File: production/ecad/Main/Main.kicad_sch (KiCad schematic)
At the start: 2 parts, among them J8 61301611821, J9 61301611821

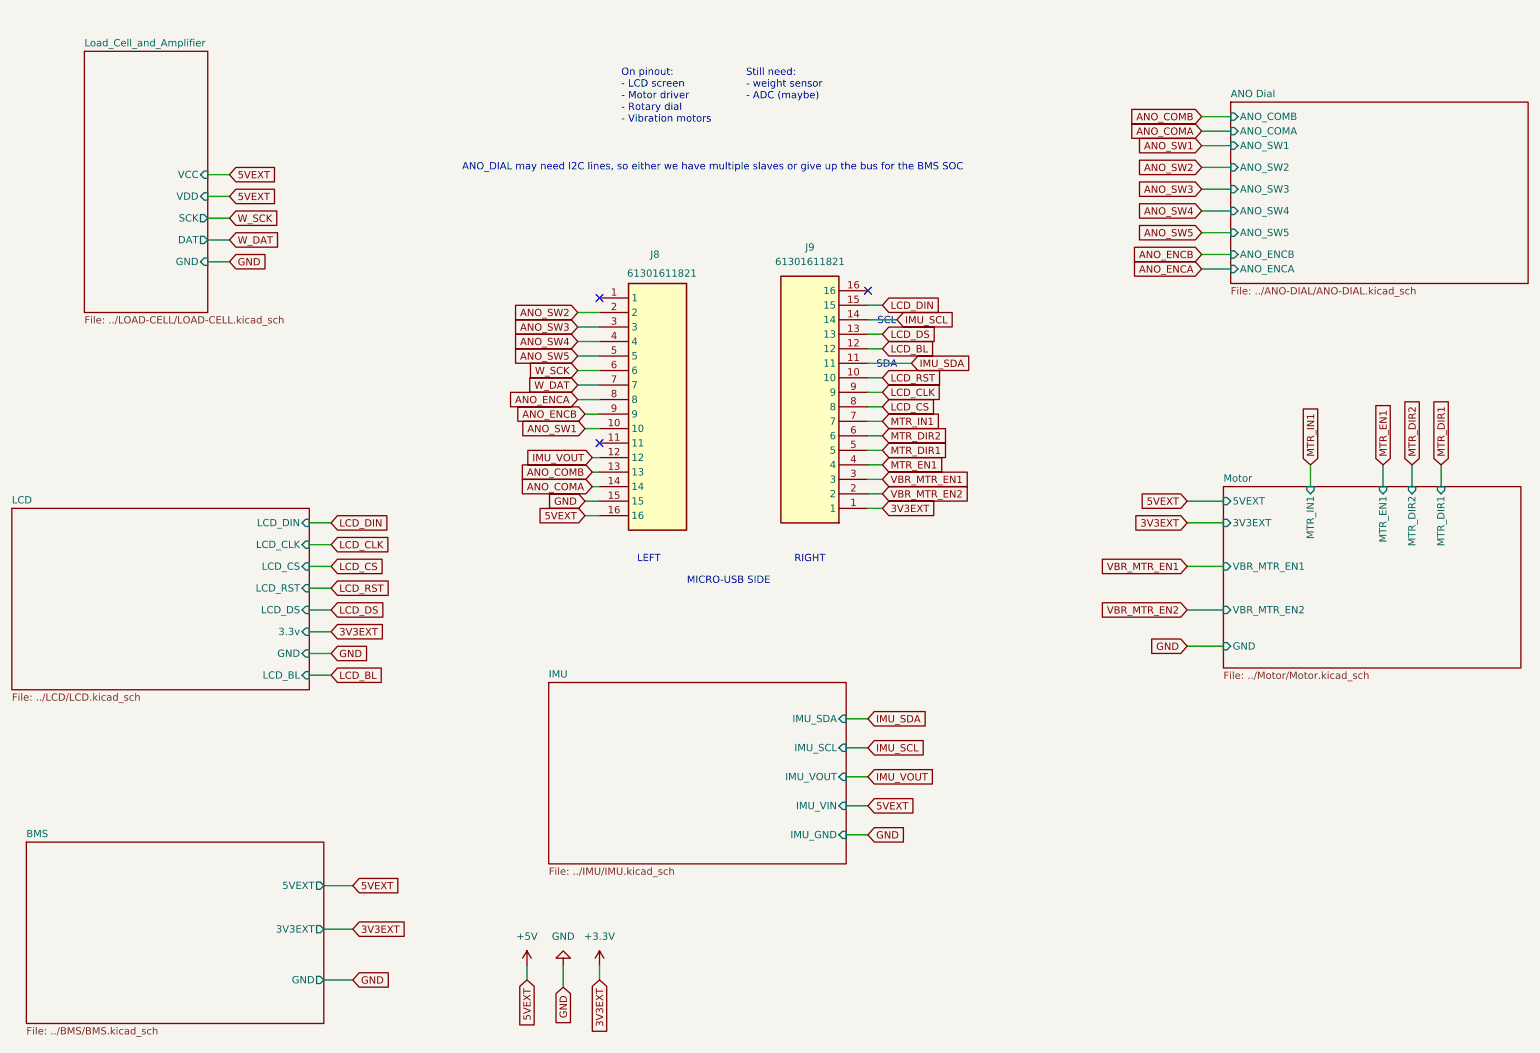
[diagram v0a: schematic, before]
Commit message: added connector for pisugar
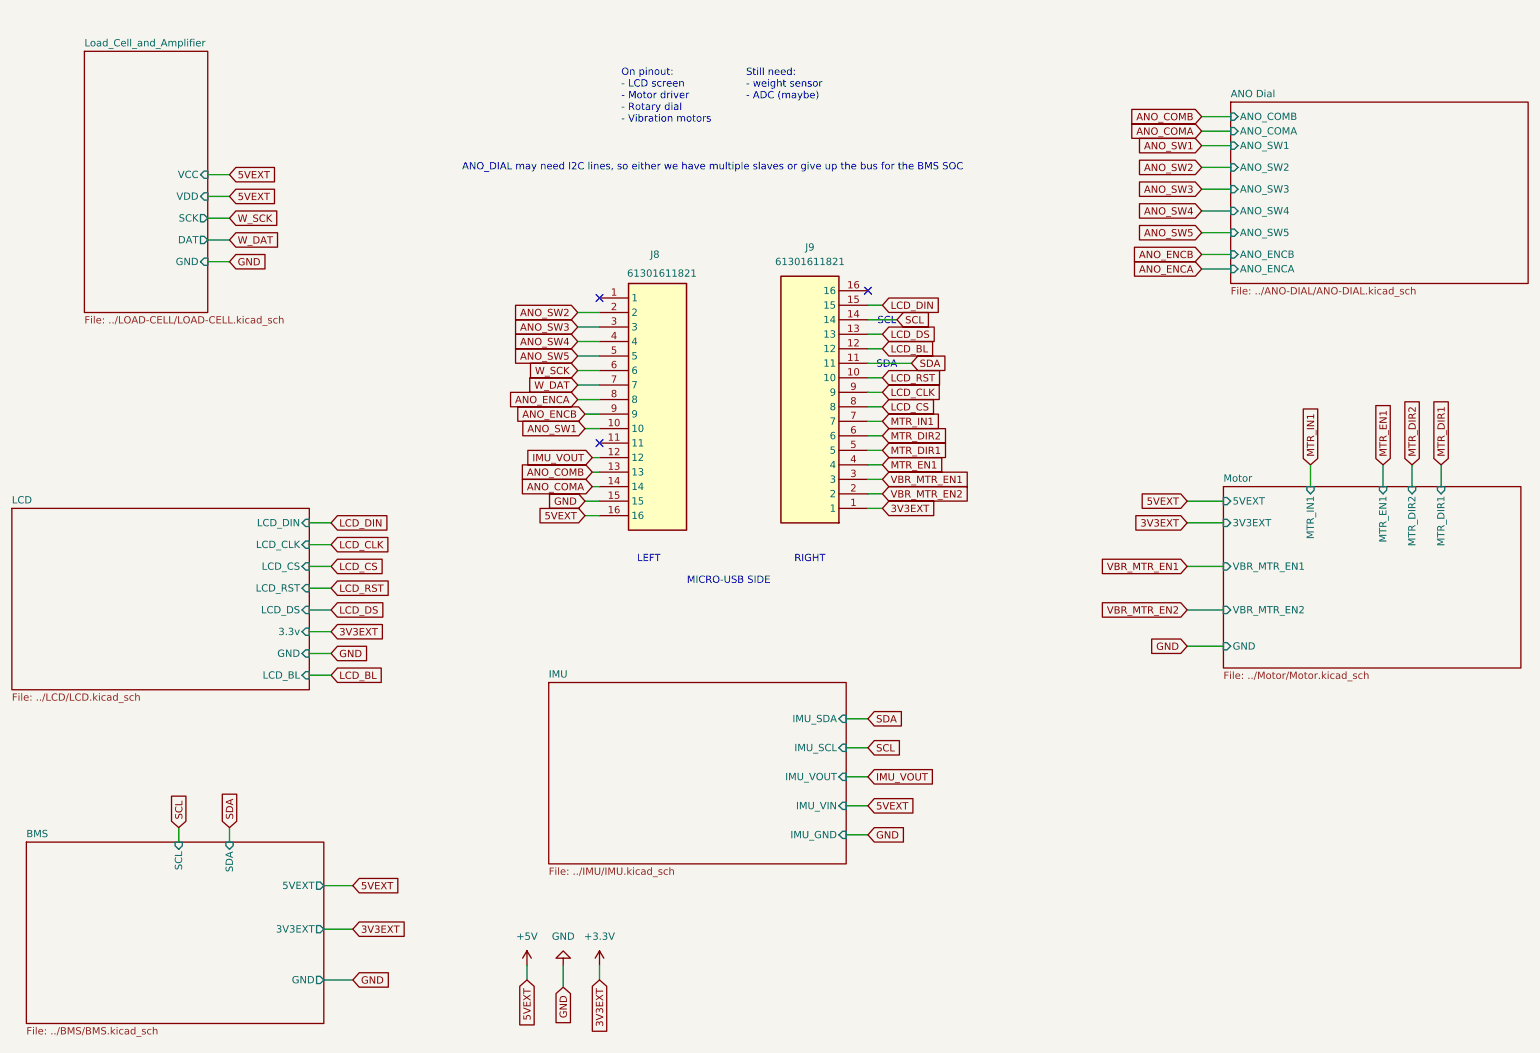
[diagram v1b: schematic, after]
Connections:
- net IMU_SCL renamed SCL
- net IMU_SDA renamed SDA
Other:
- sheet BMS ports: added SCL, SDA; removed none
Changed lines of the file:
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@@
 	(wire
 		(pts
+			(xy 45.72 156.21) (xy 45.72 158.75)
+		)
+		(stroke
+			(width 0)
+			(type default)
+		)
+	)
+	(wire
+		(pts
 			(xy 115.57 78.74) (xy 119.38 78.74)
 		)
@@
 	(wire
 		(pts
+			(xy 54.61 156.21) (xy 54.61 158.75)
+		)
+		(stroke
+			(width 0)
+			(type default)
+		)
+	)
+	(wire
+		(pts
 			(xy 50.8 53.34) (xy 54.61 53.34)
 		)
@@
 		)
 	)
-	(global_label "IMU_SDA"
+	(global_label "SDA"
 		(shape input)
 		(at 173.99 74.93 0)
@@
 		)
 		(property "Intersheetrefs" "${INTERSHEET_REFS}"
-			(at 184.8976 74.93 0)
+			(at 180.5433 74.93 0)
 			(effects
 				(font
@@
 		)
 	)
+	(global_label "SCL"
+		(shape input)
+		(at 45.72 156.21 90)
+		(fields_autoplaced yes)
+		(effects
+			(font
+				(size 1.27 1.27)
+			)
+			(justify left)
+		)
+		(property "Intersheetrefs" "${INTERSHEET_REFS}"
+			(at 45.72 149.7172 90)
+			(effects
+				(font
+					(size 1.27 1.27)
+				)
+				(justify left)
+				(hide yes)
+			)
+		)
+	)
 	(global_label "LCD_CLK"
 		(shape input)
@@
 		)
 	)
+	(global_label "SDA"
+		(shape input)
+		(at 54.61 156.21 90)
+		(fields_autoplaced yes)
+		(effects
+			(font
+				(size 1.27 1.27)
+			)
+			(justify left)
+		)
+		(property "Intersheetrefs" "${INTERSHEET_REFS}"
+			(at 54.61 149.6567 90)
+			(effects
+				(font
+					(size 1.27 1.27)
+				)
+				(justify left)
+				(hide yes)
+			)
+		)
+	)
 	(global_label "3V3EXT"
 		(shape input)
@@
 		)
 	)
-	(global_label "IMU_SDA"
+	(global_label "SDA"
 		(shape input)
 		(at 166.37 137.16 0)
@@
 		)
 		(property "Intersheetrefs" "${INTERSHEET_REFS}"
-			(at 177.2776 137.16 0)
+			(at 172.9233 137.16 0)
 			(effects
 				(font
@@
 		)
 	)
-	(global_label "IMU_SCL"
+	(global_label "SCL"
 		(shape input)
 		(at 171.45 67.31 0)
@@
 		)
 		(property "Intersheetrefs" "${INTERSHEET_REFS}"
-			(at 182.2971 67.31 0)
+			(at 177.9428 67.31 0)
 			(effects
 				(font
@@
 		)
 	)
-	(global_label "IMU_SCL"
+	(global_label "SCL"
 		(shape input)
 		(at 166.37 142.24 0)
@@
 		)
 		(property "Intersheetrefs" "${INTERSHEET_REFS}"
-			(at 177.2171 142.24 0)
+			(at 172.8628 142.24 0)
 			(effects
 				(font
@@
 			(effects
 				(font
+					(size 1.27 1.27)
+				)
+				(justify right)
+			)
+		)
+		(pin "SDA" input
+			(at 54.61 158.75 90)
+			(effects
+				(font
+					(size 1.27 1.27)
+				)
+				(justify right)
+			)
+		)
+		(pin "SCL" input
+			(at 45.72 158.75 90)
+			(effects
+				(font

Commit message: connectors
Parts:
- J8: footprint RHDR16W82P0X254_1X16_4114X250X865P -> Fitolux:15posheader
- J9: footprint RHDR16W82P0X254_1X16_4114X250X865P -> Footprints:15posheader
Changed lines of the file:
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@@
 			)
 		)
-		(property "Footprint" "RHDR16W82P0X254_1X16_4114X250X865P"
+		(property "Footprint" "Footprints:15posheader"
 			(at 149.86 5.41 0)
 			(effects
@@
 			)
 		)
-		(property "Footprint" "RHDR16W82P0X254_1X16_4114X250X865P"
+		(property "Footprint" "Fitolux:15posheader"
 			(at 135.89 158.42 0)
 			(effects

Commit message: Component placement complete
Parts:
- J8: footprint Fitolux:15posheader -> Footprints:15posheader
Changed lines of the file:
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@@
 			)
 		)
-		(property "Footprint" "Fitolux:15posheader"
+		(property "Footprint" "Footprints:15posheader"
 			(at 135.89 158.42 0)
 			(effects

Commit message: schematic changes and pcb
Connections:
- net ANO_SW1: now also J8.7; no longer J8.10
- net ANO_SW2: now also J8.6; no longer J8.2
- net W_DAT: now also J8.10; no longer J8.7
- net W_SCK: now also J8.11; no longer J8.6
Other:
- sheet ANO Dial ports: added 3V3EXT; removed none
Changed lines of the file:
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@@
 	(paper "A4")
 	(no_connect
-		(at 119.38 88.9)
-	)
-	(no_connect
 		(at 119.38 63.5)
 	)
@@
 		(at 166.37 62.23)
 	)
+	(no_connect
+		(at 119.38 66.04)
+	)
 	(wire
 		(pts
@@
 	(wire
 		(pts
+			(xy 116.84 88.9) (xy 119.38 88.9)
+		)
+		(stroke
+			(width 0)
+			(type default)
+		)
+	)
+	(wire
+		(pts
 			(xy 68.58 121.92) (xy 72.39 121.92)
 		)
@@
 	(wire
 		(pts
+			(xy 248.92 24.13) (xy 248.92 29.21)
+		)
+		(stroke
+			(width 0)
+			(type default)
+		)
+	)
+	(wire
+		(pts
 			(xy 115.57 76.2) (xy 119.38 76.2)
 		)
@@
 	(wire
 		(pts
-			(xy 115.57 66.04) (xy 119.38 66.04)
-		)
-		(stroke
-			(width 0)
-			(type default)
-		)
-	)
-	(wire
-		(pts
 			(xy 50.8 57.15) (xy 54.61 57.15)
 		)
@@
 	(global_label "W_SCK"
 		(shape input)
-		(at 115.57 76.2 180)
+		(at 116.84 88.9 180)
 		(fields_autoplaced yes)
 		(effects
@@
 		)
 		(property "Intersheetrefs" "${INTERSHEET_REFS}"
-			(at 106.4163 76.2 0)
+			(at 107.6863 88.9 0)
 			(effects
 				(font
@@
 	(global_label "ANO_SW2"
 		(shape input)
-		(at 115.57 66.04 180)
+		(at 115.57 76.2 180)
 		(fields_autoplaced yes)
 		(effects
@@
 		)
 		(property "Intersheetrefs" "${INTERSHEET_REFS}"
-			(at 103.9972 66.04 0)
+			(at 103.9972 76.2 0)
 			(effects
 				(font
@@
 		)
 	)
+	(global_label "3V3EXT"
+		(shape input)
+		(at 248.92 24.13 90)
+		(fields_autoplaced yes)
+		(effects
+			(font
+				(size 1.27 1.27)
+			)
+			(justify left)
+		)
+		(property "Intersheetrefs" "${INTERSHEET_REFS}"
+			(at 248.92 14.3111 90)
+			(effects
+				(font
+					(size 1.27 1.27)
+				)
+				(justify left)
+				(hide yes)
+			)
+		)
+	)
 	(global_label "SCL"
 		(shape input)
@@
 	(global_label "W_DAT"
 		(shape input)
-		(at 115.57 78.74 180)
+		(at 116.84 86.36 180)
 		(fields_autoplaced yes)
 		(effects
@@
 		)
 		(property "Intersheetrefs" "${INTERSHEET_REFS}"
-			(at 106.8396 78.74 0)
+			(at 108.1096 86.36 0)
 			(effects
 				(font
@@
 	(global_label "ANO_SW1"
 		(shape input)
-		(at 116.84 86.36 180)
+		(at 115.57 78.74 180)
 		(fields_autoplaced yes)
 		(effects
@@
 		)
 		(property "Intersheetrefs" "${INTERSHEET_REFS}"
-			(at 105.2672 86.36 0)
+			(at 103.9972 78.74 0)
 			(effects
 				(font
@@
 			)
 		)
+		(pin "3V3EXT" input
+			(at 248.92 29.21 90)
+			(effects
+				(font
+					(size 1.27 1.27)
+				)
+				(justify right)
+			)
+		)

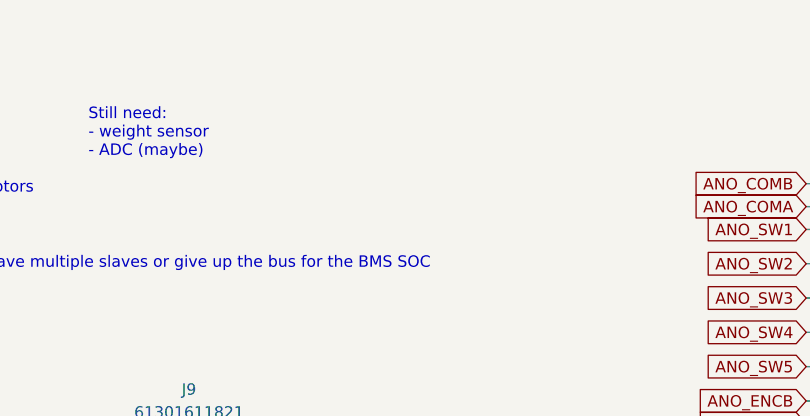
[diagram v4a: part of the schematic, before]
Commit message: Added 3V3, 5V, and GND power planes on layer 2
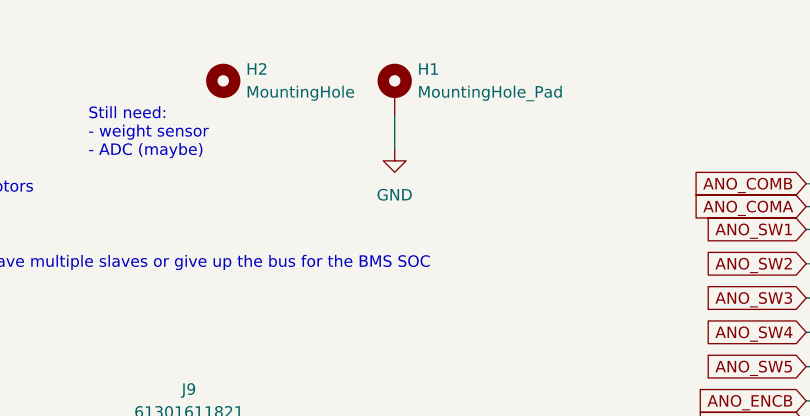
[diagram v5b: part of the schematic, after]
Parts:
- added H1: MountingHole_Pad, MountingHole:MountingHole_3.5mm_Pad, symbol Mechanical:MountingHole_Pad
- added H2: MountingHole, MountingHole:MountingHole_3.5mm, symbol Mechanical:MountingHole
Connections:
- net GND: now also H1.1
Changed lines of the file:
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@@
+	(wire
+		(pts
+			(xy 179.07 24.13) (xy 179.07 27.94)
+		)
+		(stroke
+			(width 0)
+			(type default)
+		)
+	)
 	(wire
 		(pts
@@
 	)
 	(symbol
+		(lib_id "Mechanical:MountingHole_Pad")
+		(at 179.07 21.59 0)
+		(unit 1)
+		(exclude_from_sim yes)
+		(in_bom no)
+		(on_board yes)
+		(dnp no)
+		(fields_autoplaced yes)
+		(property "Reference" "H1"
+			(at 181.61 19.0499 0)
+			(effects
+				(font
+					(size 1.27 1.27)
+				)
+				(justify left)
+			)
+		)
+		(property "Value" "MountingHole_Pad"
+			(at 181.61 21.5899 0)
+			(effects
+				(font
+					(size 1.27 1.27)
+				)
+				(justify left)
+			)
+		)
+		(property "Footprint" "MountingHole:MountingHole_3.5mm_Pad"
+			(at 179.07 21.59 0)
+			(effects
+				(font
+					(size 1.27 1.27)
+				)
+				(hide yes)
+			)
+		)
+		(property "Datasheet" "~"
+			(at 179.07 21.59 0)
+			(effects
+				(font
+					(size 1.27 1.27)
+				)
+				(hide yes)
+			)
+		)
+		(property "Description" "Mounting Hole with connection"
+			(at 179.07 21.59 0)
+			(effects
+				(font
+					(size 1.27 1.27)
+				)
+				(hide yes)
+			)
+		)
+		(pin "1"
+		)
+		(instances
+			(project ""
+				(path "/a34d77bc-8f6a-417e-a206-3165e6c5c658"
+					(reference "H1")
+					(unit 1)
+				)
+			)
+		)
+	)
+	(symbol
 		(lib_id "16positionheader:61301611821")
 		(at 166.37 100.33 180)
@@
 					(unit 1)
 				)
+			)
+		)
+	)
+	(symbol
+		(lib_id "Mechanical:MountingHole")
+		(at 160.02 20.32 0)
+		(unit 1)
+		(exclude_from_sim yes)
+		(in_bom no)
+		(on_board yes)
+		(dnp no)
+		(fields_autoplaced yes)
+		(property "Reference" "H2"
+			(at 162.56 19.0499 0)
+			(effects
+				(font
+					(size 1.27 1.27)
+				)
+				(justify left)
+			)
+		)
+		(property "Value" "MountingHole"
+			(at 162.56 21.5899 0)
+			(effects
+				(font
+					(size 1.27 1.27)
+				)
+				(justify left)
+			)
+		)
+		(property "Footprint" "MountingHole:MountingHole_3.5mm"
+			(at 160.02 20.32 0)
+			(effects
+				(font
+					(size 1.27 1.27)
+				)
+				(hide yes)
+			)
+		)
+		(property "Datasheet" "~"
+			(at 160.02 20.32 0)
+			(effects
+				(font
+					(size 1.27 1.27)
+				)
+				(hide yes)
+			)
+		)
+		(property "Description" "Mounting Hole without connection"
+			(at 160.02 20.32 0)
+			(effects
+				(font
+					(size 1.27 1.27)
+				)
+				(hide yes)
+			)
+		)
+		(instances
+			(project ""
+				(path "/a34d77bc-8f6a-417e-a206-3165e6c5c658"
+					(reference "H2")
+					(unit 1)
+				)
+			)
+		)
+	)
+	(symbol
+		(lib_id "power:GND")
+		(at 179.07 27.94 0)
+		(unit 1)
+		(exclude_from_sim no)
+		(in_bom yes)
+		(on_board yes)
+		(dnp no)
+		(fields_autoplaced yes)
+		(property "Reference" "#PWR066"
+			(at 179.07 34.29 0)
+			(effects
+				(font
+					(size 1.27 1.27)
+				)
+				(hide yes)
+			)
+		)
+		(property "Value" "GND"
+			(at 179.07 33.02 0)
+			(effects
+				(font
+					(size 1.27 1.27)
+				)
+			)
+		)
+		(property "Footprint" ""
+			(at 179.07 27.94 0)
+			(effects
+				(font
+					(size 1.27 1.27)
+				)
+				(hide yes)
+			)
+		)
+		(property "Datasheet" ""
+			(at 179.07 27.94 0)
+			(effects
+				(font
+					(size 1.27 1.27)
+				)
+				(hide yes)
+			)
+		)
+		(property "Description" "Power symbol creates a global label with name \"GND\" , ground"
+			(at 179.07 27.94 0)
+			(effects
+				(font
+					(size 1.27 1.27)
+				)
+				(hide yes)
+			)
+		)
+		(pin "1"
+		)
+		(instances
+			(project ""
+				(path "/a34d77bc-8f6a-417e-a206-3165e6c5c658"
+					(reference "#PWR066")
+					(unit 1)
+				)
